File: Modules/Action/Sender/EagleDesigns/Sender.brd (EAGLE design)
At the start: 100 x 80 mm, 10 parts, among them U2 ATMEGA328P_TQFP

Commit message: minor organizations
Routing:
- net N$2: track 4.67 -> 5.30 mm
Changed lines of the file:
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@@
 <wire x1="14.55" y1="17.05" x2="14.5" y2="17" width="0.3048" layer="16"/>
 <via x="14.5" y="17" extent="1-16" drill="0.5"/>
-<wire x1="14.5" y1="17" x2="13.47" y2="15" width="0.3048" layer="1"/>
+<wire x1="13.47" y1="15" x2="13.47" y2="16.73" width="0.3048" layer="1"/>
+<wire x1="13.47" y1="16.73" x2="13.75" y2="17.01" width="0.3048" layer="1"/>
+<wire x1="13.75" y1="17.01" x2="14.49" y2="17.01" width="0.3048" layer="1"/>
+<wire x1="14.49" y1="17.01" x2="14.5" y2="17" width="0.3048" layer="1"/>
 </signal>
 <signal name="IR-OUT">

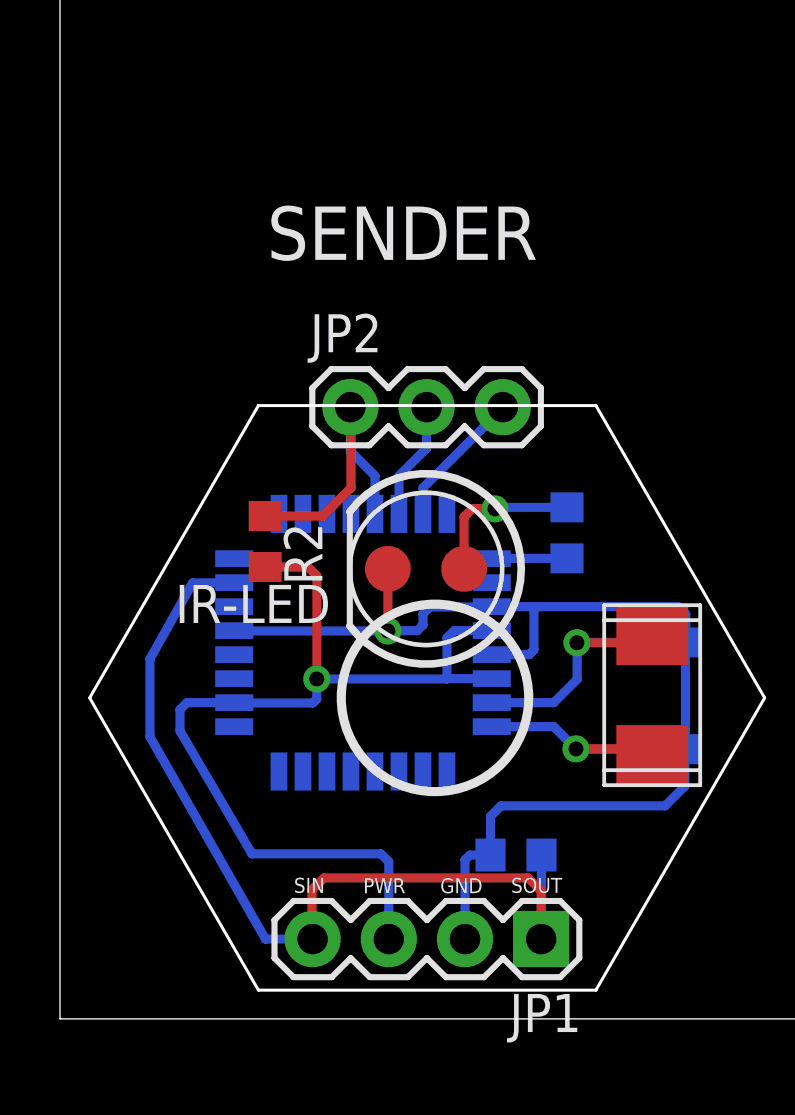
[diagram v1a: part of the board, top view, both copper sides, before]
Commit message: added version numbers, and deleted most of the text that was on each module.
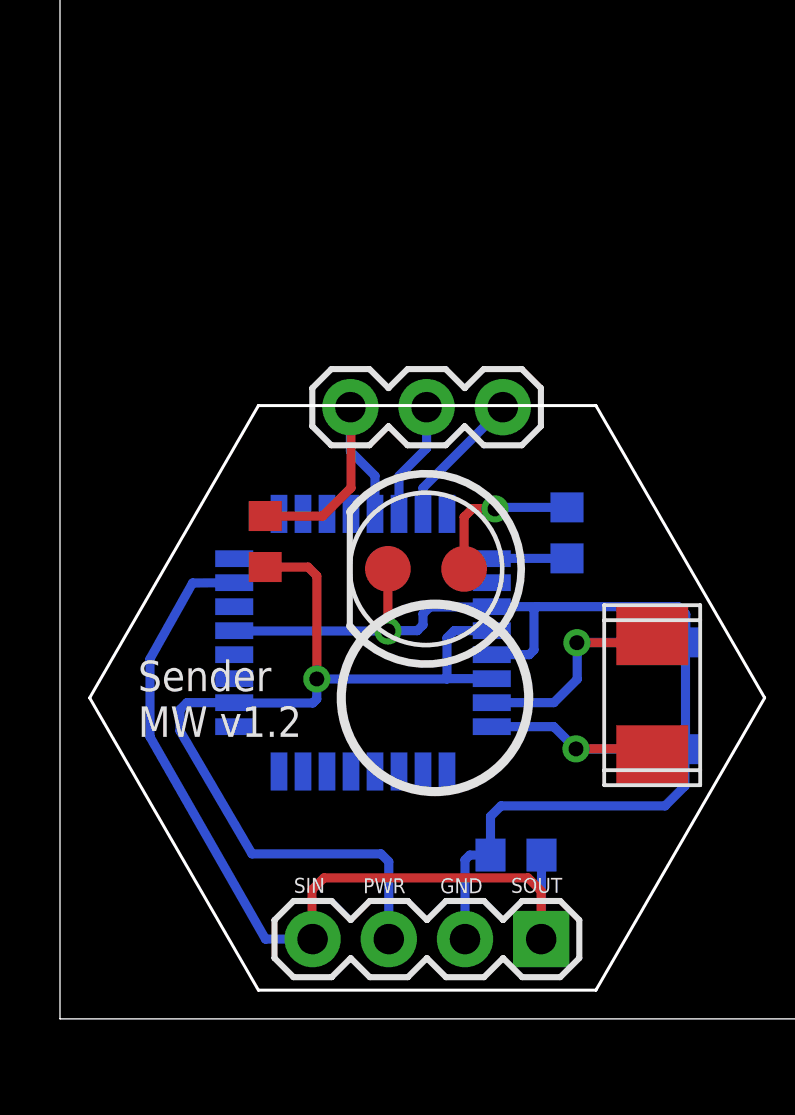
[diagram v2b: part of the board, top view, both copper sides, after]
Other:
- board text added: "Sender MW v1.2"
- board text removed: "SENDER"
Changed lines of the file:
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@@
 <layer number="19" name="Unrouted" color="6" fill="1" visible="yes" active="yes"/>
 <layer number="20" name="Dimension" color="15" fill="1" visible="yes" active="yes"/>
-<layer number="21" name="tPlace" color="7" fill="1" visible="no" active="yes"/>
-<layer number="22" name="bPlace" color="7" fill="1" visible="no" active="yes"/>
+<layer number="21" name="tPlace" color="7" fill="1" visible="yes" active="yes"/>
+<layer number="22" name="bPlace" color="7" fill="1" visible="yes" active="yes"/>
 <layer number="23" name="tOrigins" color="15" fill="1" visible="yes" active="yes"/>
 <layer number="24" name="bOrigins" color="15" fill="1" visible="yes" active="yes"/>
-<layer number="25" name="tNames" color="7" fill="1" visible="no" active="yes"/>
-<layer number="26" name="bNames" color="7" fill="1" visible="no" active="yes"/>
-<layer number="27" name="tValues" color="7" fill="1" visible="no" active="yes"/>
-<layer number="28" name="bValues" color="7" fill="1" visible="no" active="yes"/>
+<layer number="25" name="tNames" color="7" fill="1" visible="yes" active="yes"/>
+<layer number="26" name="bNames" color="7" fill="1" visible="yes" active="yes"/>
+<layer number="27" name="tValues" color="7" fill="1" visible="yes" active="yes"/>
+<layer number="28" name="bValues" color="7" fill="1" visible="yes" active="yes"/>
 <layer number="29" name="tStop" color="7" fill="3" visible="no" active="yes"/>
 <layer number="30" name="bStop" color="7" fill="6" visible="no" active="yes"/>
@@
 <text x="12.6723" y="4.188" size="0.5" layer="21">GND</text>
 <text x="15.0345" y="4.2007" size="0.5" layer="21">SOUT</text>
-<text x="6.9" y="25.3" size="1.778" layer="21">SENDER</text>
 <circle x="12.5" y="10.7" radius="3.124096875" width="0.3048" layer="21"/>
+<text x="2.6" y="9.4" size="1.016" layer="21">Sender
+MW v1.2</text>
 </plain>
 <attributes>
@@
 </autorouter>
 <elements>
-<element name="C1" library="adafruit" package="C0603" value="22pF" x="20" y="12.55" rot="MR180"/>
-<element name="C2" library="adafruit" package="C0603" value="22pF" x="19.99" y="8.99" rot="MR180"/>
-<element name="JP1" library="SparkFun-Connectors" package="1X04" value="" x="16.04" y="2.66" rot="R180"/>
-<element name="JP2" library="SparkFun-Connectors" package="1X03" value="" x="9.68" y="20.39"/>
-<element name="R1" library="adafruit" package="R0603" value="1M" x="15.2" y="5.46" rot="MR180"/>
-<element name="R2" library="resistor" package="R0603" value="10K" x="6.84" y="15.91" rot="R270"/>
-<element name="U$2" library="MakerWear" package="NX503" value="NX503" x="19.74" y="10.79" rot="R270"/>
-<element name="U2" library="SparkFun-DigitalIC" package="TQFP32-08" value="ATMEGA328P_TQFP" x="10.1" y="12.54" rot="MR0">
+<element name="C1" library="adafruit" package="C0603" value="22pF" x="20" y="12.55" smashed="yes" rot="MR180"/>
+<element name="C2" library="adafruit" package="C0603" value="22pF" x="19.99" y="8.99" smashed="yes" rot="MR180"/>
+<element name="JP1" library="SparkFun-Connectors" package="1X04" value="" x="16.04" y="2.66" smashed="yes" rot="R180">
+<attribute name="VALUE" x="17.31" y="5.835" size="1.27" layer="27" rot="R180"/>
+</element>
+<element name="JP2" library="SparkFun-Connectors" package="1X03" value="" x="9.68" y="20.39" smashed="yes">
+<attribute name="VALUE" x="8.41" y="17.215" size="1.27" layer="27"/>
+</element>
+<element name="R1" library="adafruit" package="R0603" value="1M" x="15.2" y="5.46" smashed="yes" rot="MR180"/>
+<element name="R2" library="resistor" package="R0603" value="10K" x="6.84" y="15.91" smashed="yes" rot="R270"/>
+<element name="U$2" library="MakerWear" package="NX503" value="NX503" x="19.74" y="10.79" smashed="yes" rot="R270"/>
+<element name="U2" library="SparkFun-DigitalIC" package="TQFP32-08" value="ATMEGA328P_TQFP" x="10.1" y="12.54" smashed="yes" rot="MR0">
 <attribute name="PROD_ID" value="IC-09069" x="10.1" y="12.54" size="1.778" layer="28" rot="MR0" display="off"/>
 </element>
-<element name="R3" library="adafruit" package="R0603" value="100" x="16.9" y="16.2" rot="MR270"/>
-<element name="IR-LED" library="MakerWear" package="LED5MM-SMD" value="LED-SMD" x="12.2" y="15" rot="R180"/>
+<element name="R3" library="adafruit" package="R0603" value="100" x="16.9" y="16.2" smashed="yes" rot="MR270"/>
+<element name="IR-LED" library="MakerWear" package="LED5MM-SMD" value="LED-SMD" x="12.2" y="15" smashed="yes" rot="R180"/>
 </elements>
 <signals>
@@
 </board>
 </drawing>
+<compatibility>
+<note version="6.3" minversion="6.2.2" severity="warning">
+Since Version 6.2.2 text objects can contain more than one line,
+which will not be processed correctly with this version.
+</note>
+</compatibility>
 </eagle>

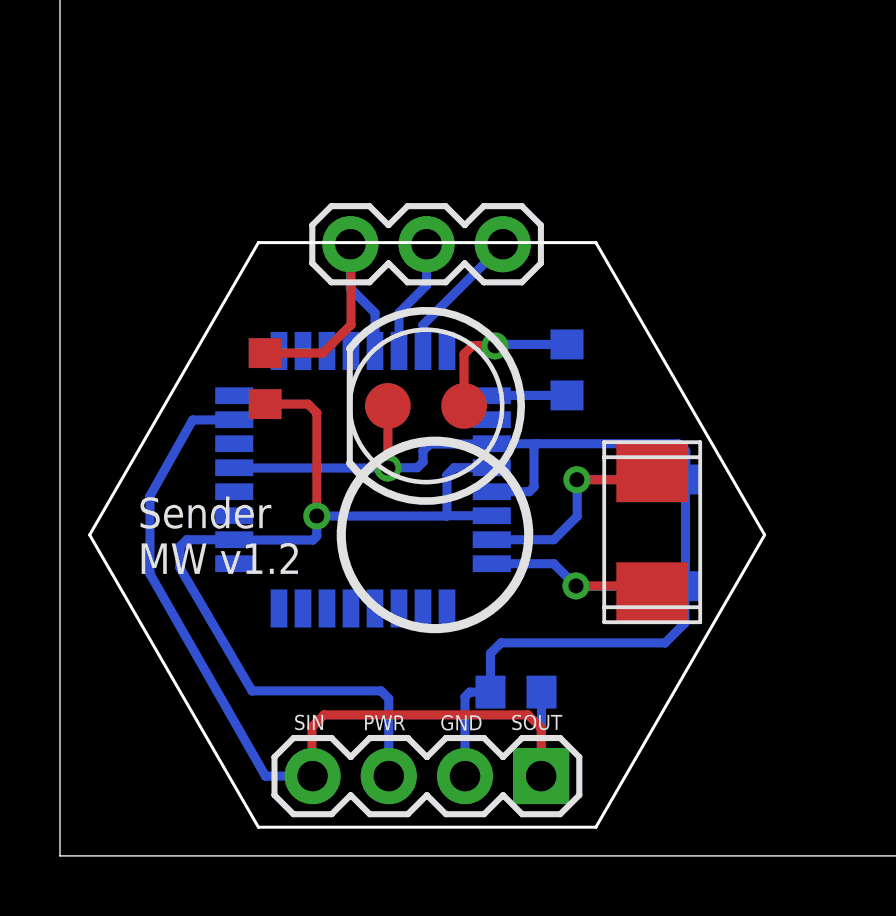
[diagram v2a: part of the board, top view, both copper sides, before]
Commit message: Sender: removed crystal, modified to work with new bootloader
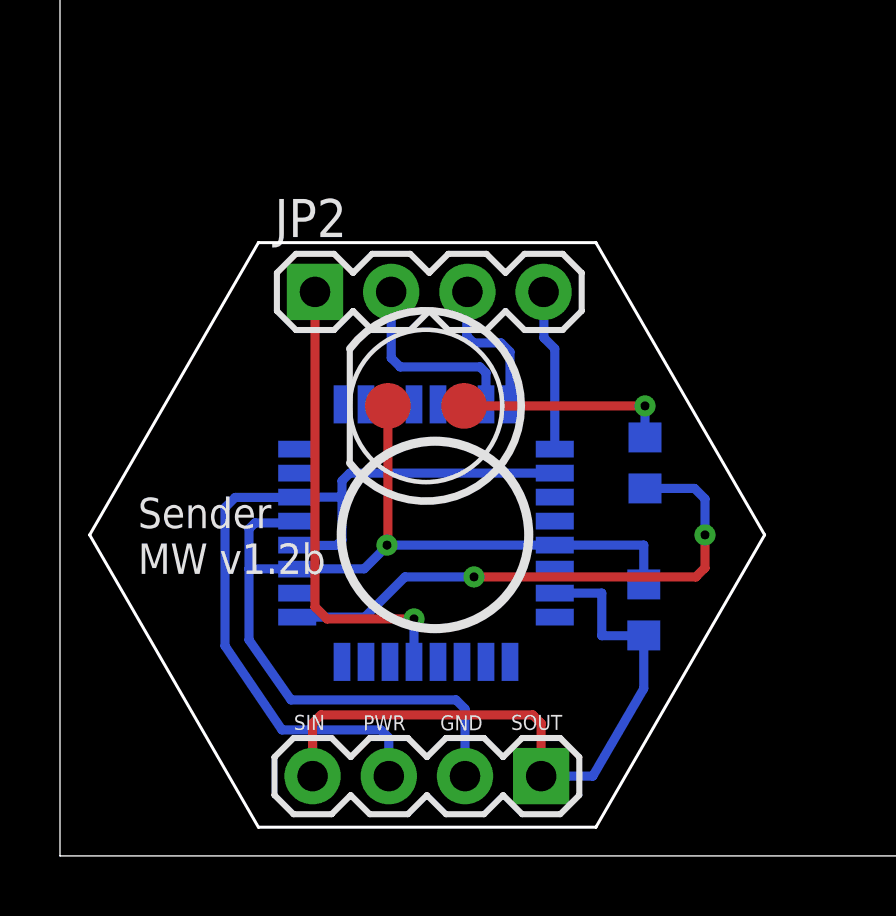
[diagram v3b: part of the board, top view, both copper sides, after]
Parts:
- removed C1, C2: 22pF, adafruit:C0603
- removed R2: 10K, resistor:R0603
- removed U$2: NX503, MakerWear:NX503
- JP2: device SparkFun-Connectors:1X03 -> SparkFun-Connectors:1X04
- moved R1 5.07 mm to (19.5, 8.20), turned to 270 degrees
- moved R3 4.05 mm to (19.5, 13.1)
- moved U2 2.75 mm to (12.2, 10.8), turned to 180 degrees
- moved JP2 1.98 mm to (8.50, 18.8)
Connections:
- removed net N$1: C1.1, U$2.P$1, U2.7
- removed net N$3: C2.1, U$2.P$2, U2.8
- removed net RX: JP2.2, U2.30
- removed net TX: JP2.3, U2.31
- new net MISO: JP2.3, U2.16
- new net MOSI: JP2.2, U2.15
- new net SCK: JP2.4, U2.17
- net GND: no longer C1.2, C2.2
- net RESET: no longer R2.1
- net VCC: no longer R2.2
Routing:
- net IR-OUT: track 2.51 -> 18.7 mm, vias 0 -> 2
- net N$1: track 8.93 -> 0.00 mm, vias 1 -> 0
- net N$3: track 7.69 -> 0.00 mm, vias 1 -> 0
- net 1X3SIN-SOUT: track 30.3 -> 22.6 mm
- net MOSI: track 0.00 -> 6.61 mm
- net RESET: track 9.84 -> 15.4 mm, vias 0 -> 1
- net SCK: track 0.00 -> 5.39 mm
- net MISO: track 0.00 -> 4.89 mm
- net TX: track 4.66 -> 0.00 mm
- net VCC: track 32.2 -> 27.8 mm, vias 1 -> 0
- net RX: track 3.94 -> 0.00 mm
- net GND: track 38.2 -> 35.5 mm
- net N$2: track 5.30 -> 7.08 mm
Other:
- board text added: "Sender MW v1.2b"
- board text removed: "Sender MW v1.2"
